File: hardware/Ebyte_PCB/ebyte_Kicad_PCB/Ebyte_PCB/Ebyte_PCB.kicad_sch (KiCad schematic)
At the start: 18 parts, among them J1 CONMMCX001, U1 LM1085IS-12/NOPB, U10 10u, U11 10u, U12 22u, U13 121, U14 365, U15 ?, U16 ?, U2 .1u, U3 DH11, U4 TPS5405DR1, U6 4.7u, U7 22u, U8 10u, U9 85.5k

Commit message: Before we destroy anything library related
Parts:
- J1: footprint CONMMCX001 -> ebyte_footprints:CONMMCX001
- U3: value DH11 -> DF11
- U4: footprint Package_SO:SOIC-8_3.9x4.9mm_P1.27mm -> ebyte_footprints:D0008A-IPC_A
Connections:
- net GND: no longer U4.7 (GND)
- net VIN: no longer U4.2 (VIN)
- net at U15.2: no longer U4.6 (COMP)
- net at U9.2: no longer U4.3 (ROSC)
- net at U8.2: no longer U4.4 (SS)
- net at U2.1: no longer U4.1 (BOOT)
- net at D1.1 (K), U2.2, U6.1: no longer U4.8 (LX)
- net at U1.1 (INPUT), U11.2, U6.2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: no longer U4.5 (VSENSE)
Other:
- moved on the sheet: U5

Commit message: fixing schem
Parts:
- J1: footprint ebyte_footprints:CONMMCX001 -> (none)
- U10, U11, U8: footprint (none) -> ebyte_footprints:C1206
- U4: value TPS5405DR1 -> TPS5405DR; footprint ebyte_footprints:D0008A-IPC_A -> D0008A-IPC_A
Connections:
- net GND: now also U14.~, U4.7 (GND), U9.~; no longer U14.1, U9.1
- net VCC: now also U13.~; no longer U13.2
- net VIN: now also U4.2 (VIN)
- net at U16.2: now also U15.~; no longer U15.1
- net at U8.2: now also U4.4 (SS)
- net at U2.1: now also U4.1 (BOOT)
- net at D1.1 (K), U2.2, U6.1: now also U4.8 (LX)
- net at U1.1 (INPUT), U11.2, U6.2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: now also U4.6 (COMP)
- net at U4.3 (ROSC): now also U9.~
- net at U4.5 (VSENSE): now also U15.~
- new net: U1.3 (ADJ/GND), U13.~, U14.~
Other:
- moved on the sheet: D1, J1, U1, U10, U11, U12, U16, U2, U3, U4, U5, U6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

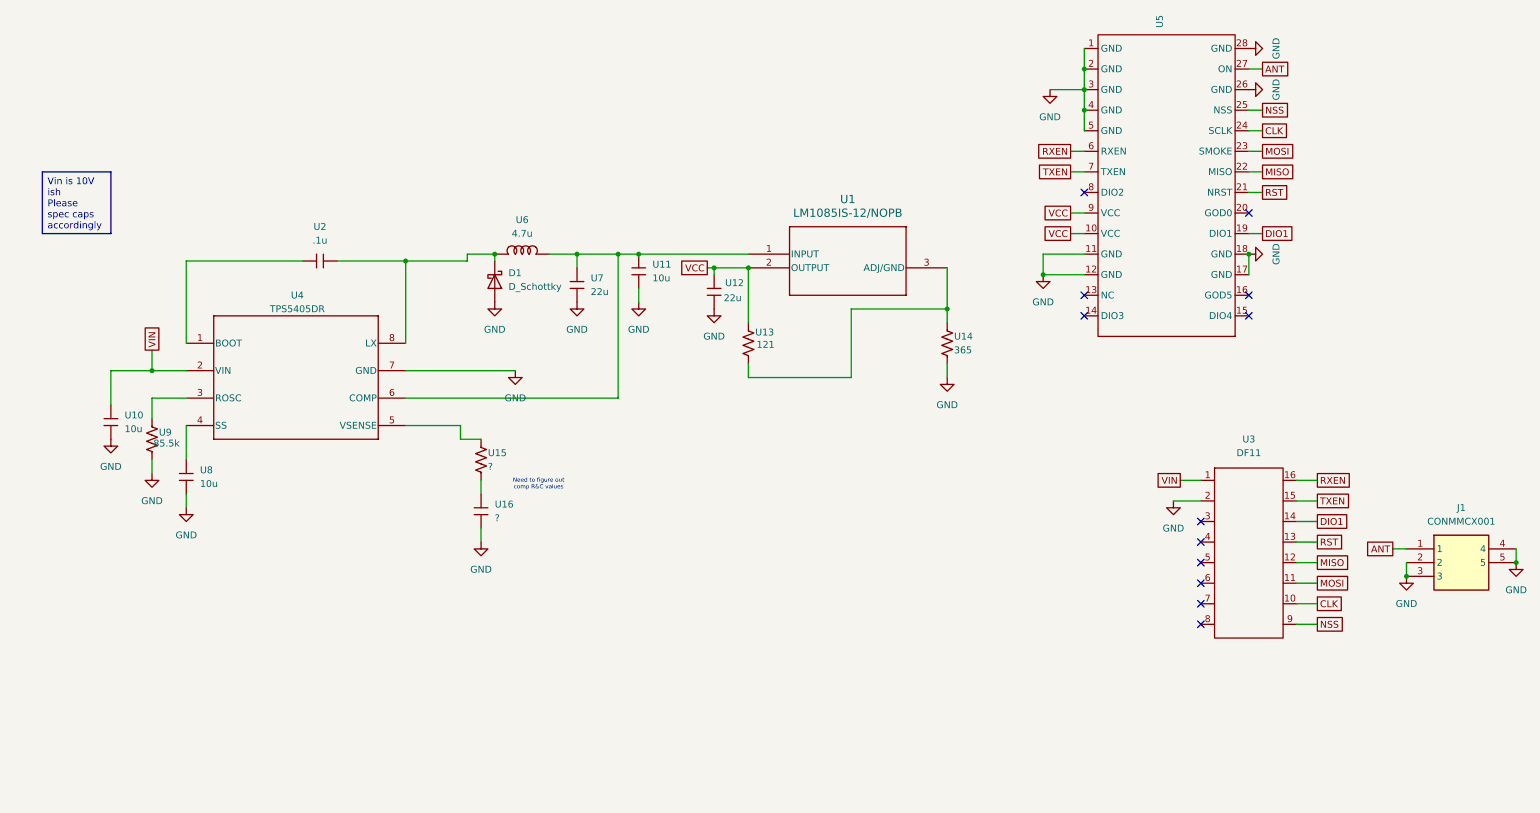
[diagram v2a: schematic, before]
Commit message: ldo/packaging
changed ldo to a rad tolerant and dropout acceptable part, added descriptions to R/L/C parts referencing package size
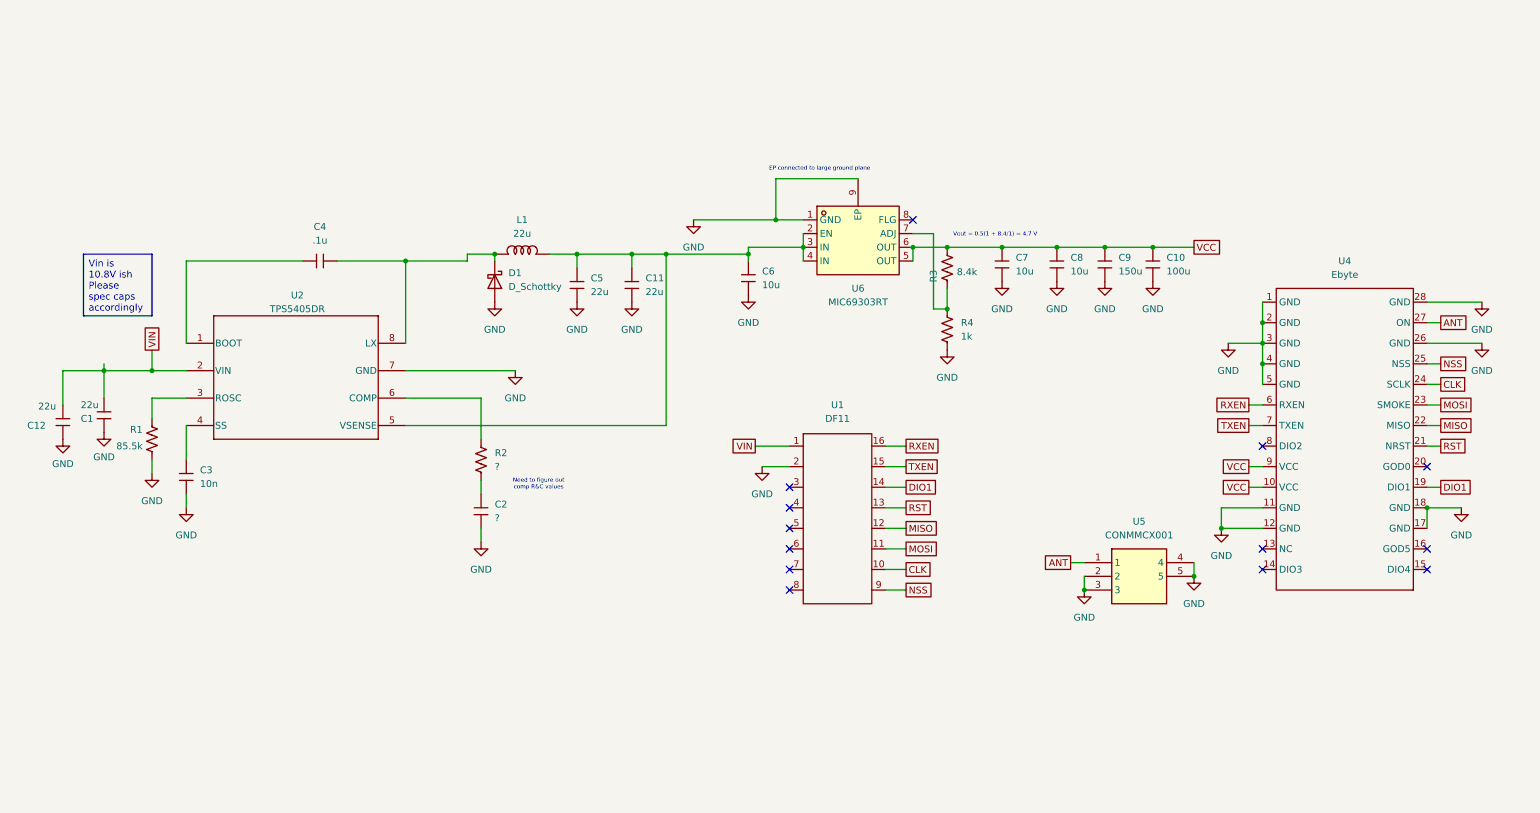
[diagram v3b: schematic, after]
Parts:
- removed U1: LM1085IS-12/NOPB, ebyte_footprints:lm1085, symbol ebyte__symbols:LM1085IS-12_NOPB
- removed U11: 10u, ebyte_footprints:C1206, symbol ebyte__symbols:Capacitor
- removed U12: 22u, symbol ebyte__symbols:Capacitor
- removed U13: 121, symbol ebyte__symbols:Resistor
- removed U14: 365, symbol ebyte__symbols:Resistor
- added C10: 100u, symbol ebyte__symbols:Capacitor
- added C11: 22u, symbol ebyte__symbols:Capacitor
- added C12: 22u, ebyte_footprints:C1206, symbol ebyte__symbols:Capacitor
- added C6, C7, C8: 10u, symbol ebyte__symbols:Capacitor
- added C9: 150u, symbol ebyte__symbols:Capacitor
- added R3: 8.4k, symbol ebyte__symbols:Resistor
- added R4: 1k, symbol ebyte__symbols:Resistor
- added U6: MIC69303RT, symbol ebyte__symbols:MIC69303RT
- C1: renamed from U10; value 10u -> 22u
- C3: renamed from U8; value 10u -> 10n
- L1: renamed from U6; value 4.7u -> 22u
- U4: renamed from U5; value ~ -> Ebyte
- renumbered U16 to C2, U2 to C4, U7 to C5, U9 to R1, U15 to R2, U3 to U1, U4 to U2, J1 to U5
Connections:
- net GND: now also C10.1, C11.1, C12.1, C6.1, C7.1, C8.1, C9.1, R4.~, U6.1 (GND), U6.9 (EP)
- net VCC: now also C10.2, C7.2, C8.2, C9.2, R3.~, U6.5 (OUT), U6.6 (OUT)
- net VIN: now also C12.2
- net at R2.~: now also C2.2; no longer U2.5 (VSENSE)
- net at C5.2, L1.2: now also U2.5 (VSENSE), C11.2, C6.2, U6.2 (EN), U6.3 (IN), U6.4 (IN); no longer U2.6 (COMP)
- new net: R2.~, U2.6 (COMP)
- new net: R3.~, R4.~, U6.7 (ADJ)
- no-connect marks 12 -> 13
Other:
- note added: "EP connected to large ground plane"
- note added: "Vout = 0.5(1 + 8.4/1) = 4.7 V"
- moved on the sheet: C1, U1, U4, U5

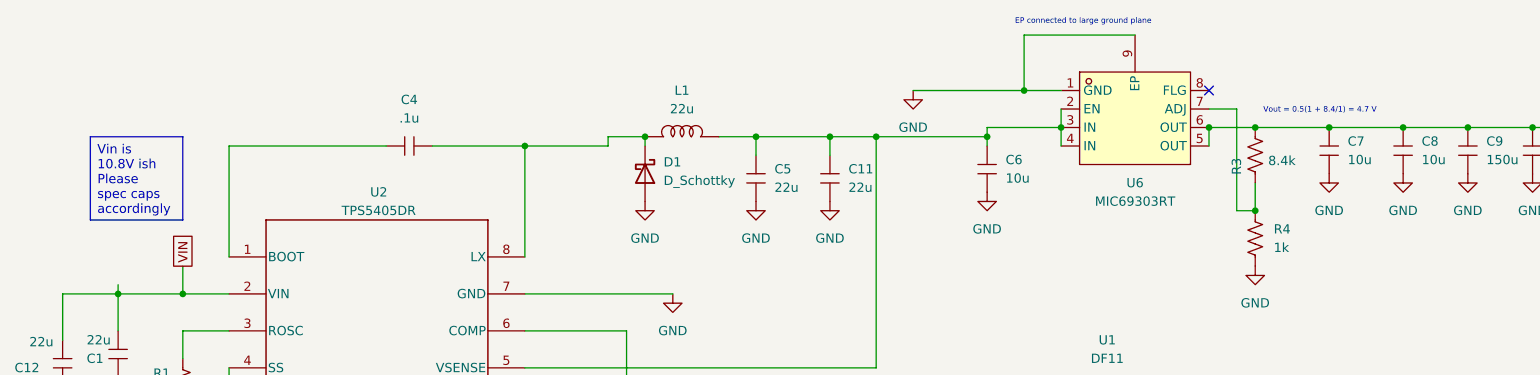
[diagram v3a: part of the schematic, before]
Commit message: assigned footprints
assigned all footprints except df11. comp r/c have temp assignments.
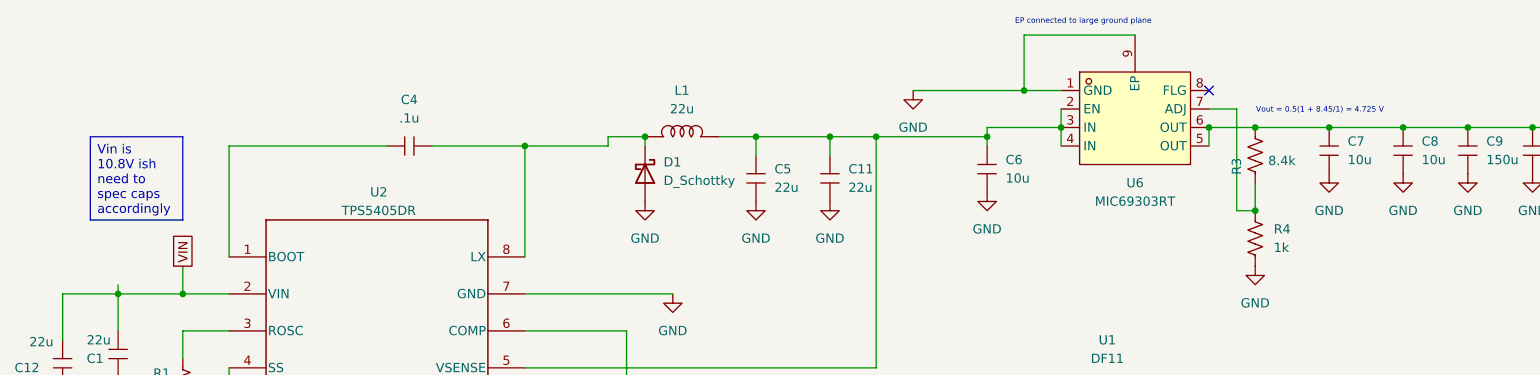
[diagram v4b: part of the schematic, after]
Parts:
- C1, C12: footprint ebyte_footprints:C1206 -> ebyte_footprints:C1210
- C10: footprint (none) -> ebyte_footprints:CAP-SMD_L7.3-W4.3-R-RD
- C11, C2, C5, C6, C7, C8: footprint (none) -> ebyte_footprints:C1206
- C3: footprint ebyte_footprints:C1206 -> ebyte_footprints:C0603
- C4: footprint (none) -> ebyte_footprints:C0603
- C9: footprint (none) -> ebyte_footprints:CAP-SMD_BD6.3-L6.6-W6.6-FD
- D1: footprint (none) -> ebyte_footprints:SMC_L7.1-W6.2-LS8.1-RD
- L1: footprint (none) -> ebyte_footprints:IND-SMD_L7.1-W6.6
- R1, R2, R3, R4: footprint (none) -> ebyte_footprints:R0603
- U2: footprint D0008A-IPC_A -> ebyte_footprints:D0008A-IPC_A
- U4: footprint (none) -> ebyte_footprints:E22-400M33S
- U5: footprint (none) -> ebyte_footprints:CONMMCX001
- U6: footprint (none) -> ebyte_footprints:SOIC-8_L4.9-W3.9-P1.27-LS6.0-BL-EP
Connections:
- new net: R3.~, R4.~, U6.7 (ADJ)
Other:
- note added: "Vout = 0.5(1 + 8.45/1) = 4.725 V"
- note removed: "Vout = 0.5(1 + 8.4/1) = 4.7 V"
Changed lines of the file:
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@@
 		)
 	)
-	(text "Vout = 0.5(1 + 8.4/1) = 4.7 V"
+	(text "Vout = 0.5(1 + 8.45/1) = 4.725 V"
 		(exclude_from_sim no)
 		(at 190.5 87.884 0)
@@
 		)
 	)
-	(text_box "Vin is 10.8V ish\nPlease spec caps accordingly"
+	(text_box "Vin is 10.8V ish\nneed to  spec caps accordingly"
 		(exclude_from_sim no)
 		(at 21.59 91.44 0)
@@
 			)
 		)
-		(property "Footprint" ""
+		(property "Footprint" "ebyte_footprints:CONMMCX001"
 			(at 223.52 243.51 0)
 			(effects
@@
 			)
 		)
-		(property "Footprint" "ebyte_footprints:C1206"
+		(property "Footprint" "ebyte_footprints:C1210"
 			(at 25.4 120.65 0)
 			(effects
@@
 			)
 		)
-		(property "Footprint" ""
+		(property "Footprint" "ebyte_footprints:R0603"
 			(at 95.25 129.54 0)
 			(effects
@@
 			)
 		)
-		(property "Footprint" ""
+		(property "Footprint" "ebyte_footprints:R0603"
 			(at 34.29 125.73 0)
 			(effects
@@
 			)
 		)
-		(property "Footprint" "ebyte_footprints:C1206"
+		(property "Footprint" "ebyte_footprints:C0603"
 			(at 40.64 132.08 0)
 			(effects
@@
 			)
 		)
-		(property "Footprint" "ebyte_footprints:C1206"
+		(property "Footprint" "ebyte_footprints:C1210"
 			(at 17.78 121.92 0)
 			(effects
@@
 			)
 		)
-		(property "Footprint" ""
+		(property "Footprint" "ebyte_footprints:C1206"
 			(at 191.77 92.71 0)
 			(effects
@@
 			)
 		)
-		(property "Footprint" ""
+		(property "Footprint" "ebyte_footprints:E22-400M33S"
 			(at 255.27 125.73 0)
 			(effects
@@
 			)
 		)
-		(property "Footprint" ""
+		(property "Footprint" "ebyte_footprints:CAP-SMD_L7.3-W4.3-R-RD"
 			(at 219.71 92.71 0)
 			(effects
@@
 			)
 		)
-		(property "Footprint" ""
+		(property "Footprint" "ebyte_footprints:C1206"
 			(at 123.19 96.52 0)
 			(effects
@@
 			)
 		)
-		(property "Footprint" ""
+		(property "Footprint" "ebyte_footprints:CAP-SMD_BD6.3-L6.6-W6.6-FD"
 			(at 210.82 92.71 0)
 			(effects
@@
 			)
 		)
-		(property "Footprint" ""
+		(property "Footprint" "ebyte_footprints:C0603"
 			(at 66.04 92.71 0)
 			(effects
@@
 			)
 		)
-		(property "Footprint" ""
+		(property "Footprint" "ebyte_footprints:SOIC-8_L4.9-W3.9-P1.27-LS6.0-BL-EP"
 			(at 165.1 88.9 0)
 			(effects
@@
 			)
 		)
-		(property "Footprint" ""
+		(property "Footprint" "ebyte_footprints:C1206"
 			(at 201.93 92.71 0)
 			(effects
@@
 			)
 		)
-		(property "Footprint" ""
+		(property "Footprint" "ebyte_footprints:R0603"
 			(at 181.61 105.41 0)
 			(effects
@@
 			)
 		)
-		(property "Footprint" ""
+		(property "Footprint" "ebyte_footprints:C1206"
 			(at 144.78 95.25 0)
 			(effects
@@
 			)
 		)
-		(property "Footprint" ""
+		(property "Footprint" "ebyte_footprints:R0603"
 			(at 181.61 93.98 0)
 			(effects
@@
 			)
 		)
-		(property "Footprint" ""
+		(property "Footprint" "ebyte_footprints:SMC_L7.1-W6.2-LS8.1-RD"
 			(at 97.79 96.52 0)
 			(effects
@@
 			)
 		)
-		(property "Footprint" ""
+		(property "Footprint" "ebyte_footprints:IND-SMD_L7.1-W6.6"
 			(at 102.87 91.44 0)
 			(effects
@@
 			)
 		)
-		(property "Footprint" ""
+		(property "Footprint" "ebyte_footprints:C1206"
 			(at 113.03 96.52 0)
 			(effects
@@
 			)
 		)
-		(property "Footprint" "D0008A-IPC_A"
+		(property "Footprint" "ebyte_footprints:D0008A-IPC_A"
 			(at 40.64 107.95 0)
 			(effects
@@
 			)
 		)
-		(property "Footprint" ""
+		(property "Footprint" "ebyte_footprints:C1206"
 			(at 95.25 138.43 0)
 			(effects

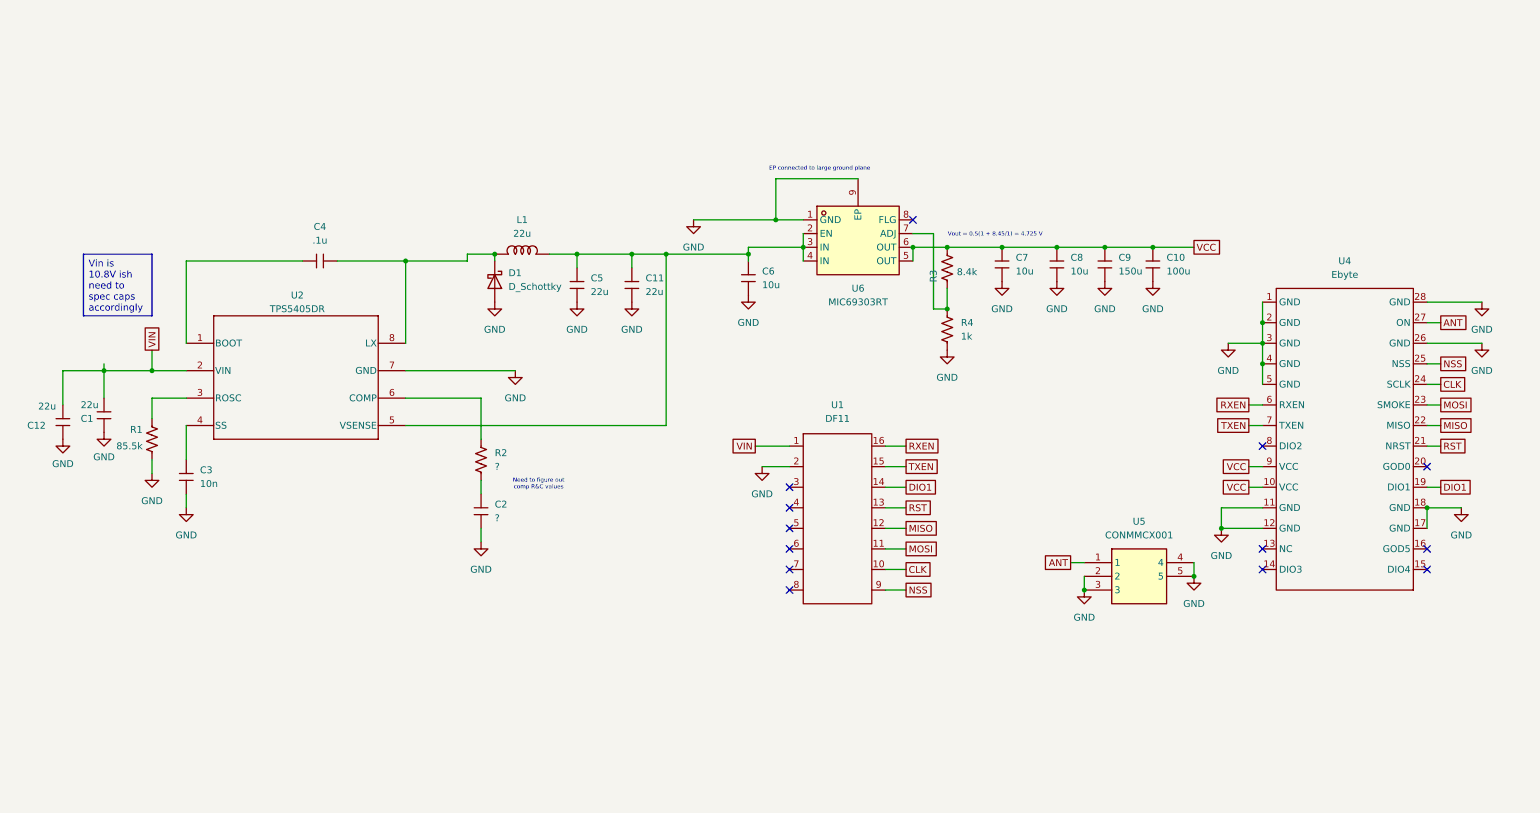
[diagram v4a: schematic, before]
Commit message: PCB Layout
initial layout done. df11 connector on left, buck cluster top left. unsure if ldo cluster should be close to buck output or ebyte vcc, or just somewhere in between.  ant connector isolated by ebyte.
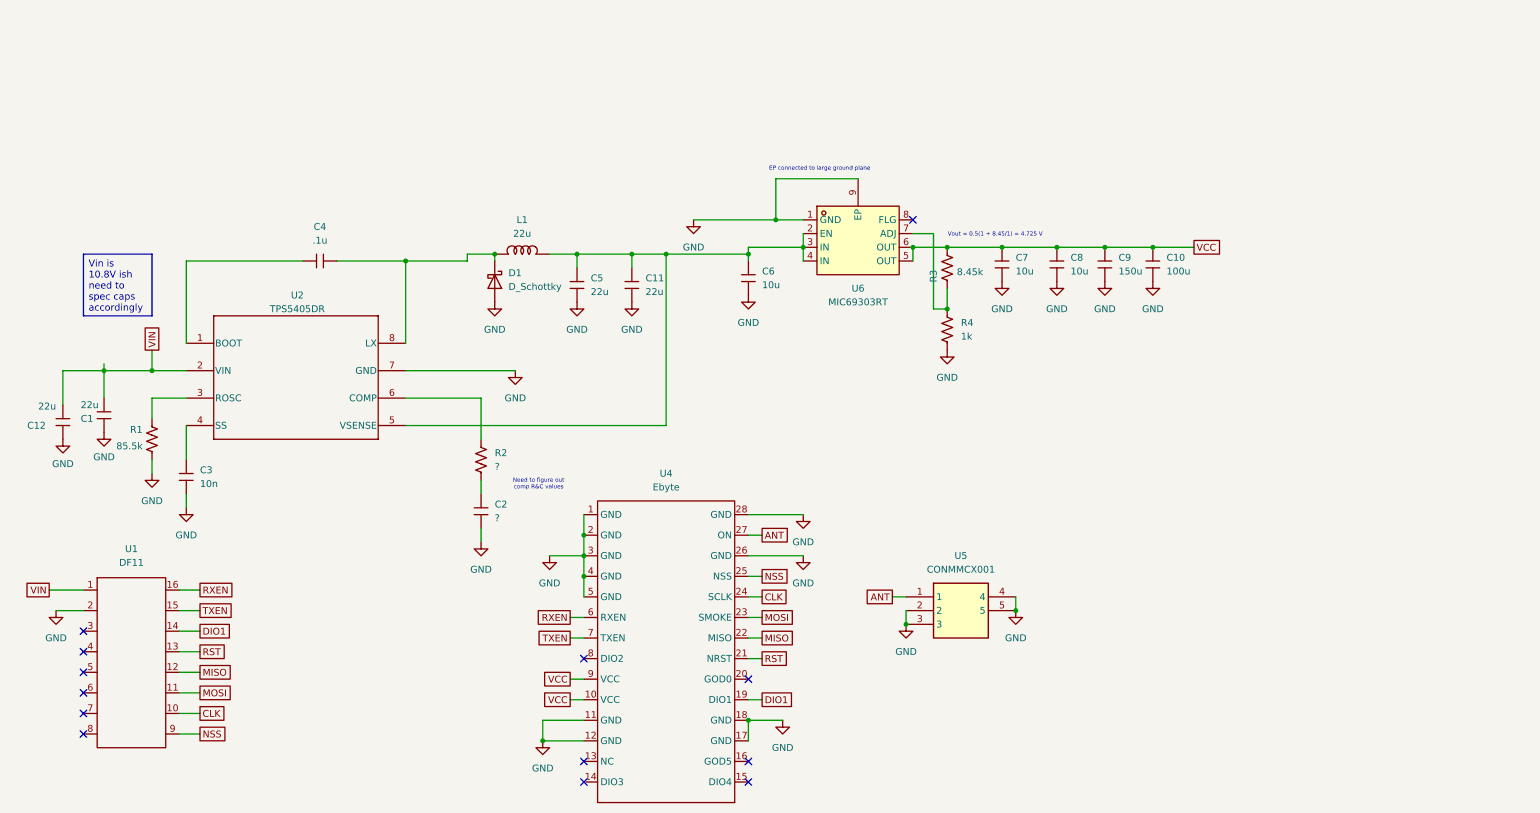
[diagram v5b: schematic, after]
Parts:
- R3: value 8.4k -> 8.45k
- U1: footprint (none) -> ebyte_footprints:Hirose_DF11-16DP-2DSA_2x08_P2.00mm_Vertical
- U2: footprint ebyte_footprints:D0008A-IPC_A -> D0008A-IPC_A
- U5: footprint ebyte_footprints:CONMMCX001 -> CONMMCX001
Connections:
- net GND: now also R1.1, R4.1; no longer R1.~, R4.~
- net VCC: now also R3.2; no longer R3.~
- net at U2.6 (COMP): now also R2.2; no longer R2.~
- net at C2.2: now also R2.1; no longer R2.~
- net at U2.3 (ROSC): now also R1.2; no longer R1.~
- new net: R3.1, R4.2, U6.7 (ADJ)
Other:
- moved on the sheet: U1, U4, U5

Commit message: Updated schematic
fixed ebyte, found Comp values, added termination resistor.
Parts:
- added R5: 22, ebyte_footprints:R0603, symbol ebyte__symbols:Resistor
- C2: value ? -> 4.7n; footprint ebyte_footprints:C1206 -> ebyte_footprints:C0603
- R2: value ? -> 33k
- U2: footprint D0008A-IPC_A -> ebyte_footprints:D0008A-IPC_A
- U5: footprint CONMMCX001 -> ebyte_footprints:CONMMCX001
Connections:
- net CLK: no longer U1.10
- net DIO1: no longer U1.14
- net GND: now also U1.11, U1.12, U1.13, U1.14, U1.15, U1.16; no longer U1.2
- net MISO: no longer U1.12
- net MOSI: no longer U1.11
- net NSS: no longer U1.9
- net RST: no longer U1.13
- net RXEN: no longer U1.16
- net TXEN: no longer U1.15
- net VIN: no longer U1.1
- net at U1.3: now also R5.2
- net GPIO1_26: now reaches U1.4
- net SPI1SDI: now reaches U1.5
- net GPIO1_27: now reaches U1.6
- net SPI1_SCK: now reaches U1.7
- net GPIO1_28: now reaches U1.8
- new net GPIO1_25: U1.2
- new net GPIO1_29: U1.10
- new net SPI1_CS1: U1.1
- new net SPI1_SDO: R5.1
- new net X_PGOOD: U1.9
- no-connect marks 13 -> 7
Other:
- note removed: "Need to figure out comp R&C values"
- moved on the sheet: U1
